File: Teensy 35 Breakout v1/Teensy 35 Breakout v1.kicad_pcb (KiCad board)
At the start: 2 copper layers, 99.1 x 106.7 mm, 41 parts, among them P1 CONN_01X13, P10 CONN_01X13, P10a1 CONN_01X10, P11 CONN_01X03, P12 CONN_01X04, P13 CONN_02X04, P14 CONN_02X03, P15 CONN_02X05, P16 CONN_01X03, P17 CONN_01X01, P18 CONN_01X02, P19 CONN_01X08, P1a1 CONN_01X09, P2 CONN_01X13, P20 CONN_01X05, P21 CONN_01X05, P22 CONN_01X04, P23 CONN_01X04, P24 CONN_01X05, P25 CONN_01X10, P26 CONN_01X10, P27 CONN_01X10, P28 CONN_01X10, P2a1 CONN_01X09, P2a2 CONN_01X03, P2a3 CONN_01X03, P3 CONN_01X03, P4 CONN_01X24, P5 CONN_01X24, P6 CONN_01X03, P7 CONN_01X24, P8 CONN_01X24, P9 CONN_01X13, P9a1 CONN_01X09, SW1 SW_PUSH_SMALL_H, SW2 SW_PUSH_SMALL_H

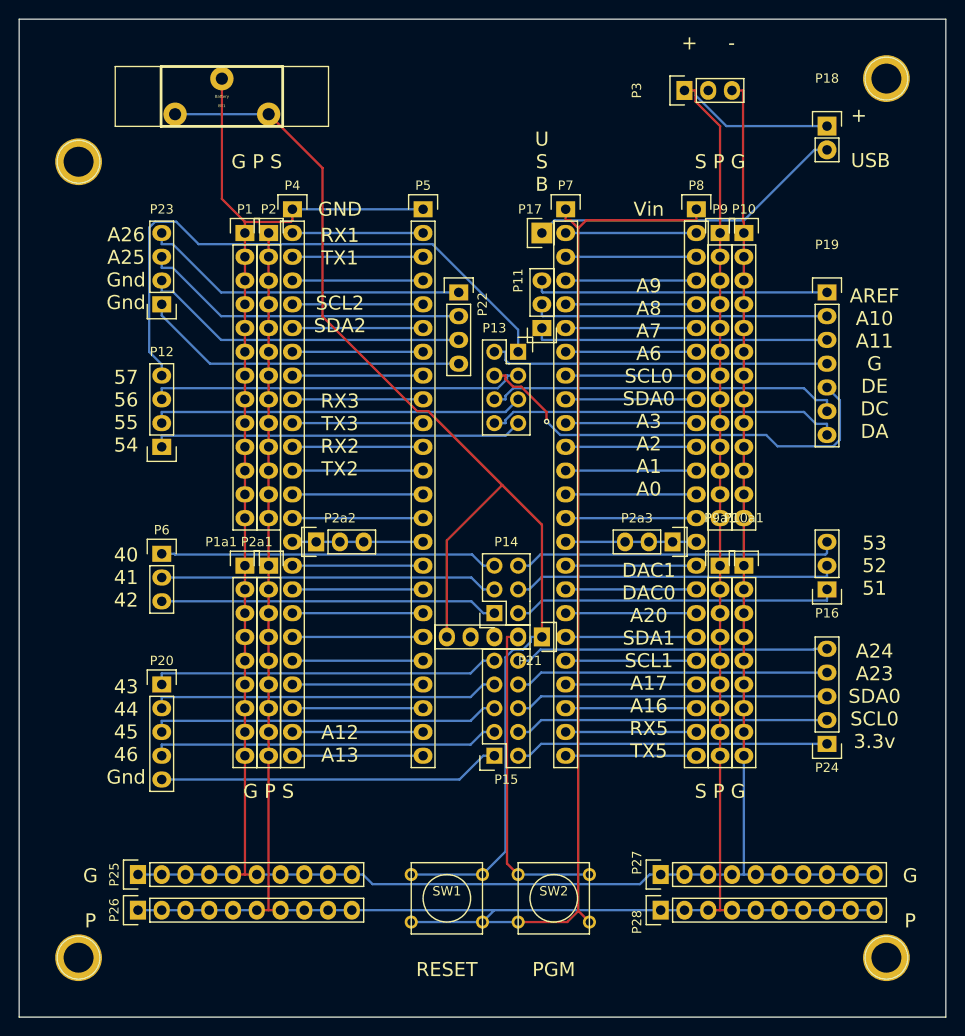
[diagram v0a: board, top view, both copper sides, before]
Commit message: corrected reset voltage to 3.3v
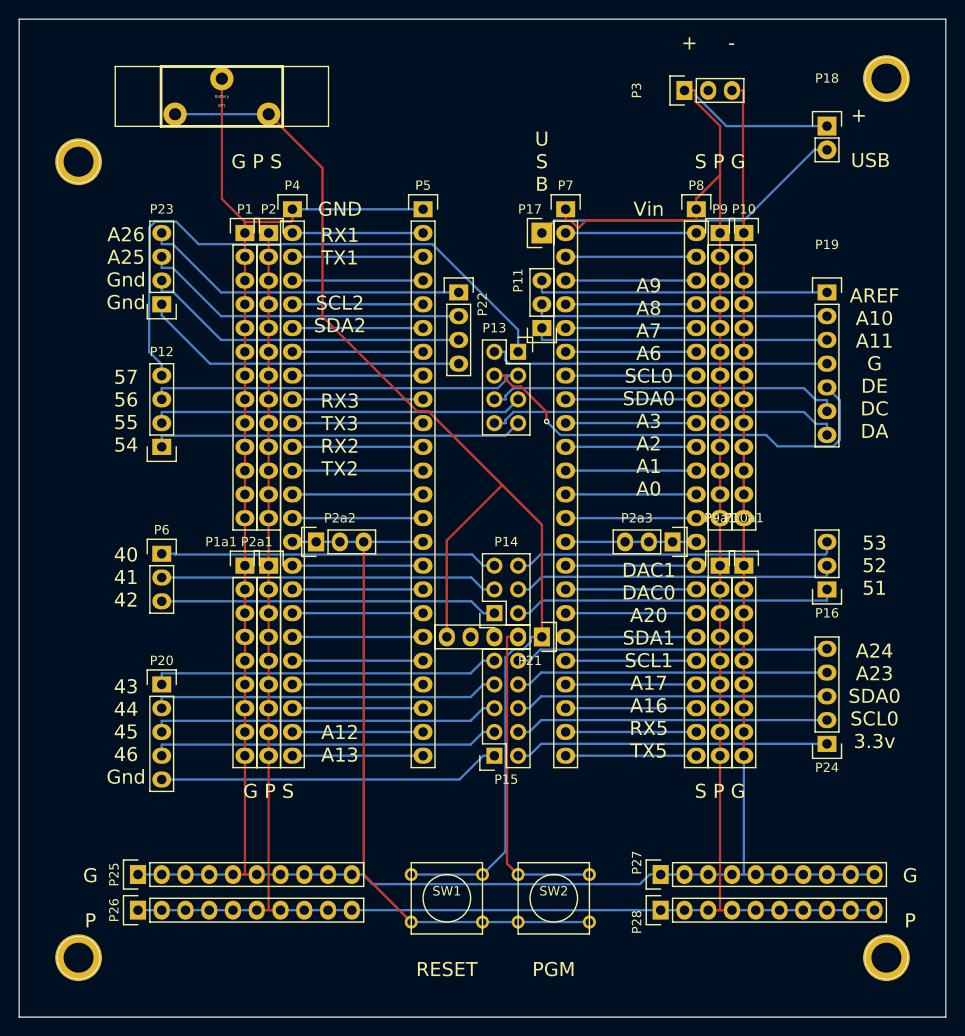
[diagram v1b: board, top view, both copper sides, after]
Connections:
- P7 pad 1: Net-(P18-Pad1) -> Net-(P7-Pad1)
- SW1 pad 2: Net-(P18-Pad1) -> Net-(P2a2-Pad1)
- SW2 pad 2: Net-(P18-Pad1) -> Net-(P2a2-Pad1)
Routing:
- net Net-(P18-Pad1): track 370.0 -> 278.2 mm
- net Net-(P2a2-Pad1): track 14.0 -> 75.8 mm
- net Net-(P7-Pad1): track 0.00 -> 1.71 mm

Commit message: Additional corrections
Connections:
- SW1 pad 2: Net-(P2a2-Pad1) -> Net-(P2a3-Pad1)
- SW2 pad 2: Net-(P2a2-Pad1) -> Net-(P2a3-Pad1)
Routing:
- net Net-(P2a2-Pad1): track 75.8 -> 14.0 mm
- net Net-(P2a3-Pad1): track 14.0 -> 74.8 mm
- net Net-(P18-Pad1): track 278.2 -> 278.8 mm
- net Net-(P7-Pad1): track 1.71 -> 1.19 mm
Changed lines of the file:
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@@
   (general
     (links 227)
-    (no_connects 3)
+    (no_connects 1)
     (area 60.909999 30.429999 160.070001 137.210001)
     (thickness 1.6)
     (drawings 29)
-    (tracks 383)
+    (tracks 385)
     (zones 0)
     (modules 41)
@@
   (layers
     (0 F.Cu signal)
-    (31 B.Cu signal)
+    (31 B.Cu signal hide)
     (32 B.Adhes user)
     (33 F.Adhes user)
@@
       (net 79 "Net-(P21-Pad1)"))
     (pad 2 thru_hole circle (at 3.81 2.54) (size 1.397 1.397) (drill 0.8128) (layers *.Cu *.Mask F.SilkS)
-      (net 4 "Net-(P2a2-Pad1)"))
+      (net 5 "Net-(P2a3-Pad1)"))
     (pad 1 thru_hole circle (at -3.81 -2.54) (size 1.397 1.397) (drill 0.8128) (layers *.Cu *.Mask F.SilkS)
       (net 79 "Net-(P21-Pad1)"))
     (pad 2 thru_hole circle (at -3.81 2.54) (size 1.397 1.397) (drill 0.8128) (layers *.Cu *.Mask F.SilkS)
-      (net 4 "Net-(P2a2-Pad1)"))
+      (net 5 "Net-(P2a3-Pad1)"))
   )
   (module Buttons_Switches_ThroughHole:SW_PUSH_SMALL (layer F.Cu)
@@
       (net 80 "Net-(P21-Pad2)"))
     (pad 2 thru_hole circle (at 3.81 2.54) (size 1.397 1.397) (drill 0.8128) (layers *.Cu *.Mask F.SilkS)
-      (net 4 "Net-(P2a2-Pad1)"))
+      (net 5 "Net-(P2a3-Pad1)"))
     (pad 1 thru_hole circle (at -3.81 -2.54) (size 1.397 1.397) (drill 0.8128) (layers *.Cu *.Mask F.SilkS)
       (net 80 "Net-(P21-Pad2)"))
     (pad 2 thru_hole circle (at -3.81 2.54) (size 1.397 1.397) (drill 0.8128) (layers *.Cu *.Mask F.SilkS)
-      (net 4 "Net-(P2a2-Pad1)"))
+      (net 5 "Net-(P2a3-Pad1)"))
   )
   (module Pin_Headers:Pin_Header_Straight_1x03 (layer F.Cu)
@@
   (segment (start 87.63 125.73) (end 87.63 109.22) (width 0.25) (layer F.Cu) (net 3))
   (segment (start 135.89 125.73) (end 135.89 109.22) (width 0.25) (layer F.Cu) (net 3))
-  (segment (start 120.731 52.8197) (end 119.9 51.9889) (width 0.25) (layer F.Cu) (net 3))
   (segment (start 121.562 51.9889) (end 120.731 52.8197) (width 0.25) (layer F.Cu) (net 3))
   (segment (start 133.35 51.9889) (end 121.562 51.9889) (width 0.25) (layer F.Cu) (net 3))
@@
   (segment (start 135.89 47.1431) (end 133.422 49.6111) (width 0.25) (layer F.Cu) (net 3))
   (segment (start 133.35 50.8) (end 133.35 49.6111) (width 0.25) (layer F.Cu) (net 3))
-  (segment (start 102.87 127) (end 110.49 127) (width 0.25) (layer B.Cu) (net 4))
+  (segment (start 120.731 52.8197) (end 119.9 51.9889) (width 0.25) (layer F.Cu) (net 3))
+  (segment (start 119.9 51.9889) (end 119.38 51.9889) (width 0.25) (layer F.Cu) (net 3))
   (segment (start 90.17 86.36) (end 92.71 86.36) (width 0.25) (layer B.Cu) (net 4))
   (segment (start 104.14 86.36) (end 97.79 86.36) (width 0.25) (layer B.Cu) (net 4))
   (segment (start 97.79 86.36) (end 95.25 86.36) (width 0.25) (layer B.Cu) (net 4))
   (segment (start 95.25 86.36) (end 92.71 86.36) (width 0.25) (layer B.Cu) (net 4))
-  (segment (start 97.79 121.92) (end 102.87 127) (width 0.25) (layer F.Cu) (net 4))
-  (segment (start 97.79 86.36) (end 97.79 121.92) (width 0.25) (layer F.Cu) (net 4))
-  (segment (start 114.3 127) (end 110.49 127) (width 0.25) (layer B.Cu) (net 4))
-  (segment (start 114.3 127) (end 121.92 127) (width 0.25) (layer B.Cu) (net 4))
+  (segment (start 121.92 127) (end 120.72101 125.80101) (width 0.25) (layer F.Cu) (net 5))
+  (segment (start 120.72101 125.80101) (end 120.72101 87.54861) (width 0.25) (layer F.Cu) (net 5))
+  (segment (start 120.72101 87.54861) (end 119.5324 86.36) (width 0.25) (layer F.Cu) (net 5))
+  (segment (start 119.5324 86.36) (end 119.38 86.36) (width 0.25) (layer F.Cu) (net 5))
+  (segment (start 102.87 127) (end 110.49 127) (width 0.25) (layer B.Cu) (net 5))
+  (segment (start 114.3 127) (end 110.49 127) (width 0.25) (layer B.Cu) (net 5))
+  (segment (start 114.3 127) (end 121.92 127) (width 0.25) (layer B.Cu) (net 5))
   (segment (start 133.35 86.36) (end 130.81 86.36) (width 0.25) (layer B.Cu) (net 5))
   (segment (start 119.38 86.36) (end 125.73 86.36) (width 0.25) (layer B.Cu) (net 5))
@@
   (segment (start 76.2 60.96) (end 76.2 62.1489) (width 0.25) (layer B.Cu) (net 86))
   (segment (start 119.38 51.9889) (end 119.38 50.8) (width 0.25) (layer F.Cu) (net 87))
-  (segment (start 119.9 51.9889) (end 119.38 51.9889) (width 0.25) (layer F.Cu) (net 87))
 )
